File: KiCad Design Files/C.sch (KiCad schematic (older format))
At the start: 16 parts, among them Q1 2N3904, Q2 2N3904

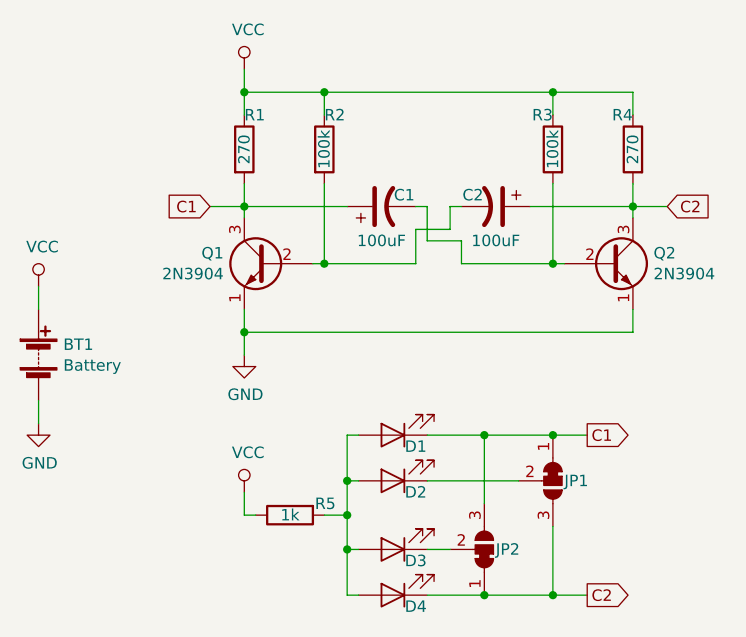
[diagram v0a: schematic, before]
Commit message: Updated schematic, 100k to 10k. Added right title block
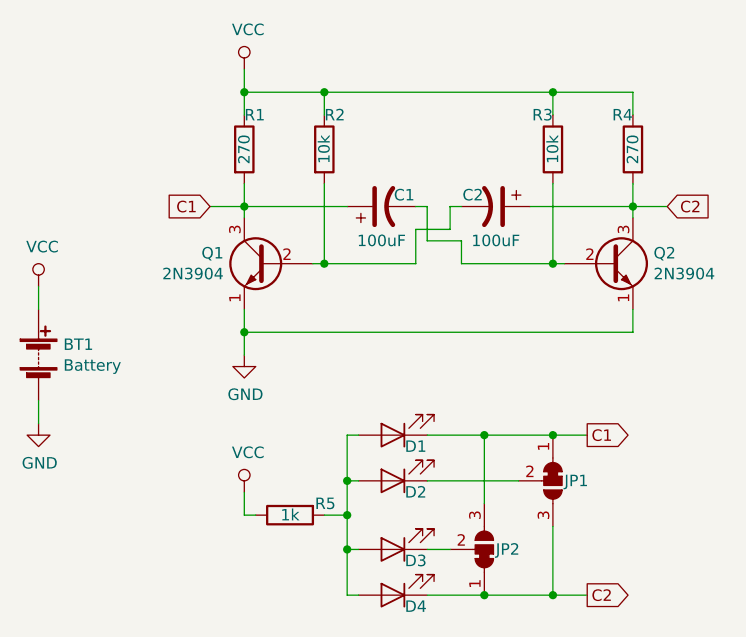
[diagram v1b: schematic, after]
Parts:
- R2, R3: value 100k -> 10k
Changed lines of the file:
@@
 P 2500 1300
 F 0 "R2" H 2500 1450 50  0000 L CNN
-F 1 "100k" V 2500 1300 50  0000 C CNN
+F 1 "10k" V 2500 1300 50  0000 C CNN
 F 2 "Resistor_THT:R_Axial_DIN0207_L6.3mm_D2.5mm_P10.16mm_Horizontal" V 2430 1300 50  0001 C CNN
 F 3 "~" H 2500 1300 50  0001 C CNN
@@
 P 3500 1300
 F 0 "R3" H 3500 1450 50  0000 L CNN
-F 1 "100k" V 3500 1300 50  0000 C CNN
+F 1 "10k" V 3500 1300 50  0000 C CNN
 F 2 "Resistor_THT:R_Axial_DIN0207_L6.3mm_D2.5mm_P10.16mm_Horizontal" V 3430 1300 50  0001 C CNN
 F 3 "~" H 3500 1300 50  0001 C CNN
